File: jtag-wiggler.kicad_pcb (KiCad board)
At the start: 2 copper layers, 152.4 x 101.6 mm, 50 parts, among them J1 DSUB-25_Male_Horizontal_P2.77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, J2 BarrelJack_Horizontal, P1 PinHeader_1x02_P2.54mm_Vertic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, P2 PinHeader_1x03_P2.54mm_Vertic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, P3 PinHeader_1x08_P2.54mm_Vertic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, Q1 TO-92_Wide, SW1 SW_NKK_G1xJP, U1 DIP-20_W7.62mm_Socket_LongPads, U2 TO-220-3_Vertical, U3 TO-220-3_Vertical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

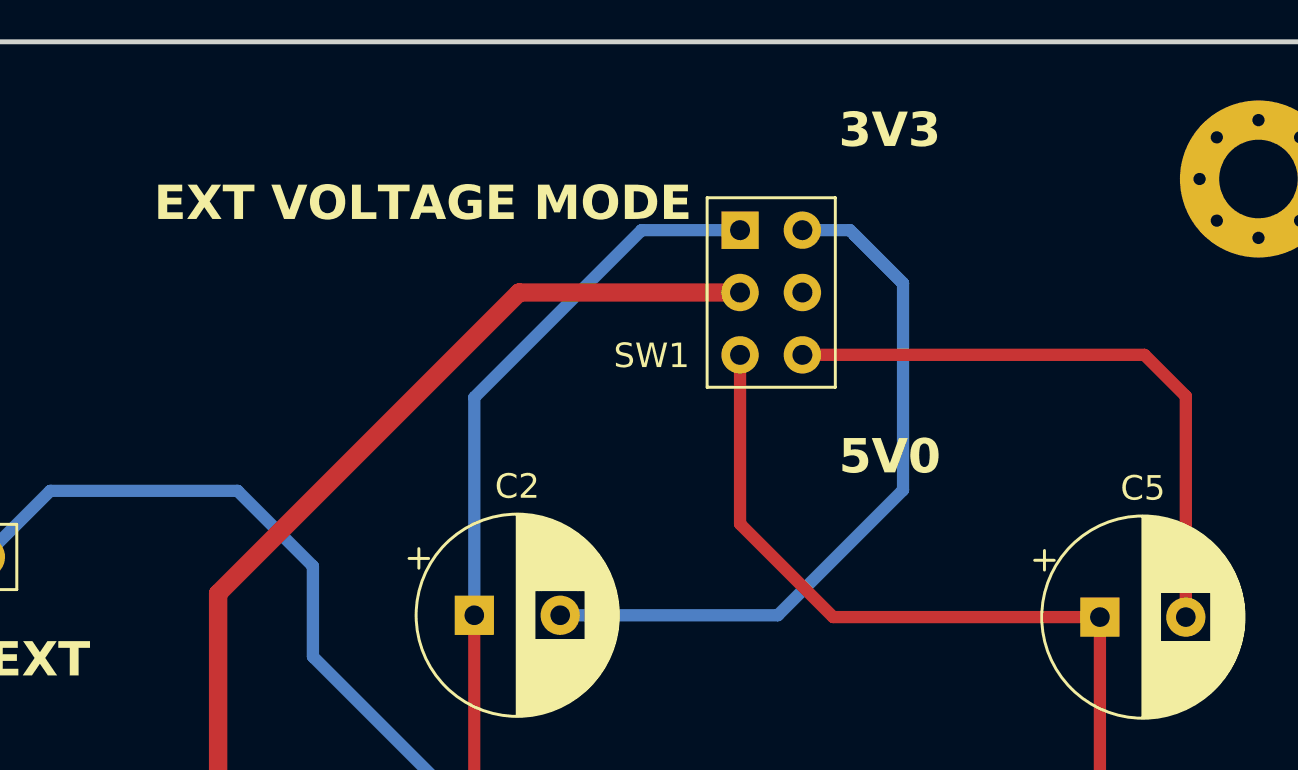
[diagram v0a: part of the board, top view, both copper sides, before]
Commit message: Add custom switch footprint; update PCB layout
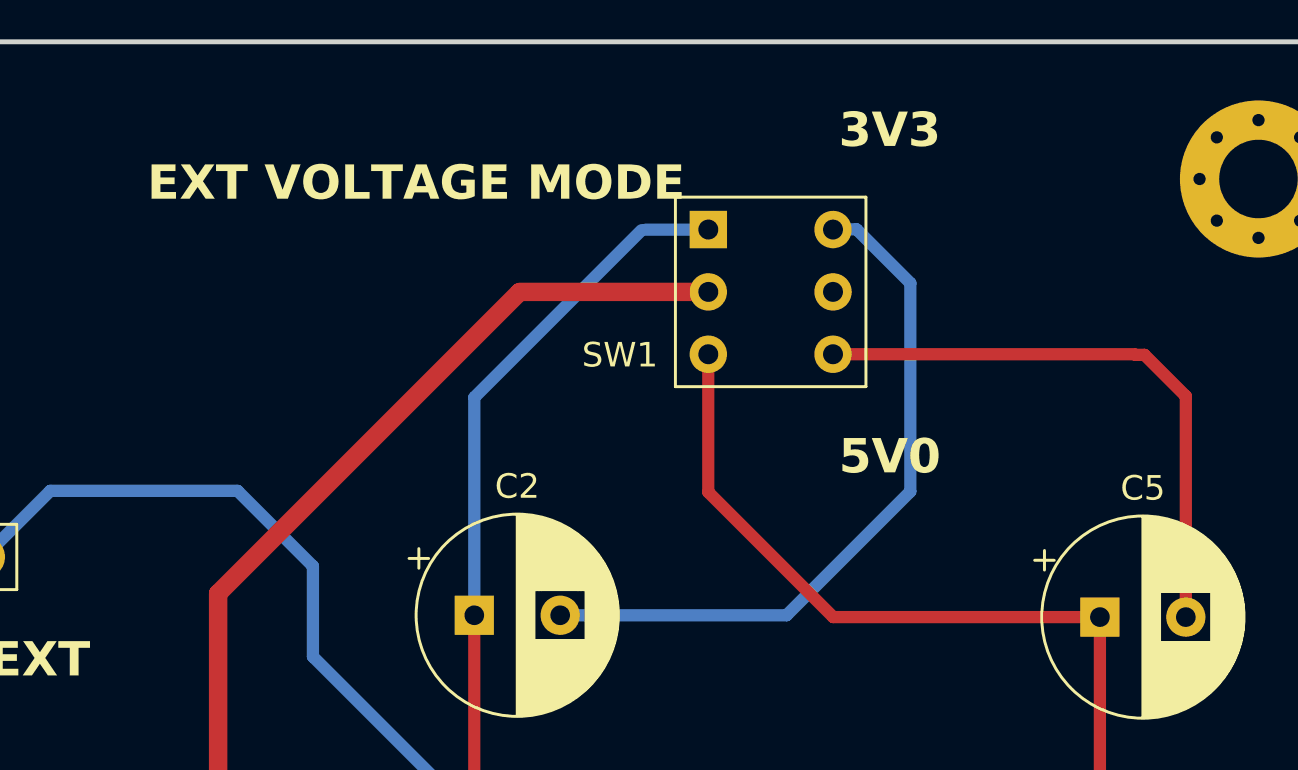
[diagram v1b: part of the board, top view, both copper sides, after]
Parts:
- SW1: value SW_NKK_G1xJP -> SW_Generic; footprint Button_Switch_THT:SW_NKK_G1xJP -> Switches:SW_Generic
- moved SW1 1.29 mm to (198.2, 55.9)
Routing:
- net C2_negative: track 32.3 -> 28.9 mm
- net C2_positive: track 46.7 -> 45.2 mm
- net Protected_VCC: track 74.7 -> 73.5 mm
- net C5_negative: track 25.3 -> 24.1 mm
- net C5_positive: track 34.7 -> 35.3 mm
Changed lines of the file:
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@@
     )
   )
-  (footprint "Button_Switch_THT:SW_NKK_G1xJP" (layer "F.Cu")
-    (at 199.477707 55.935)
-    (descr "Switch NKK G1xJP http://www.nkkswitches.com/pdf/gwillum.pdf")
-    (tags "SWITCH TOGGLE ILLUM SPDT NKK")
+  (footprint "Switches:SW_Generic" (layer "F.Cu")
+    (at 198.185 55.91)
+    (descr "Generic Switch - 2.54mm x 5.08mm spacing")
+    (tags "SWITCH TOGGLE DPDT")
     (attr through_hole)
     (fp_text reference "SW1" (at -3.602707 5.115) (layer "F.SilkS")
         (effects (font (size 1 1) (thickness 0.15)))
     )
-    (fp_text value "SW_NKK_G1xJP" (at 1.27 7.3) (layer "F.Fab")
+    (fp_text value "SW_Generic" (at 2.54 7.3) (layer "F.Fab")
         (effects (font (size 1 1) (thickness 0.15)))
     )
-    (fp_text user "${REFERENCE}" (at 1.27 -2.2) (layer "F.Fab")
+    (fp_text user "${REFERENCE}" (at 2.54 -2.2) (layer "F.Fab")
         (effects (font (size 1 1) (thickness 0.15)))
     )
-    (fp_line (start -1.34112 -1.3208) (end 3.88112 -1.3208)
+    (fp_line (start -1.34112 -1.3208) (end 6.42112 -1.3208)
       (stroke (width 0.12) (type solid)) (layer "F.SilkS"))
     (fp_line (start -1.34112 6.4008) (end -1.34112 -1.3208)
       (stroke (width 0.12) (type solid)) (layer "F.SilkS"))
-    (fp_line (start -1.34112 6.4008) (end 3.88112 6.4008)
+    (fp_line (start -1.34112 6.4008) (end 6.42112 6.4008)
       (stroke (width 0.12) (type solid)) (layer "F.SilkS"))
-    (fp_line (start 3.88112 -1.3208) (end 3.88112 6.4008)
+    (fp_line (start 6.42112 -1.3208) (end 6.42112 6.4008)
       (stroke (width 0.12) (type solid)) (layer "F.SilkS"))
     (fp_line (start -1.48 6.54) (end -1.48 -1.46)
       (stroke (width 0.05) (type solid)) (layer "F.CrtYd"))
-    (fp_line (start -1.48 6.54) (end 4.02 6.54)
+    (fp_line (start -1.48 6.54) (end 6.56 6.54)
       (stroke (width 0.05) (type solid)) (layer "F.CrtYd"))
-    (fp_line (start 4.02 -1.46) (end -1.48 -1.46)
+    (fp_line (start 6.56 -1.46) (end -1.48 -1.46)
       (stroke (width 0.05) (type solid)) (layer "F.CrtYd"))
-    (fp_line (start 4.02 -1.46) (end 4.02 6.54)
+    (fp_line (start 6.56 -1.46) (end 6.56 6.54)
       (stroke (width 0.05) (type solid)) (layer "F.CrtYd"))
-    (fp_line (start -1.23 -1.21) (end 3.77 -1.21)
+    (fp_line (start -1.23 -1.21) (end 6.31 -1.21)
       (stroke (width 0.1) (type solid)) (layer "F.Fab"))
     (fp_line (start -1.23 6.29) (end -1.23 -1.21)
       (stroke (width 0.1) (type solid)) (layer "F.Fab"))
-    (fp_line (start -1.23 6.29) (end 3.77 6.29)
+    (fp_line (start -1.23 6.29) (end 6.31 6.29)
       (stroke (width 0.1) (type solid)) (layer "F.Fab"))
-    (fp_line (start 3.77 6.29) (end 3.77 -1.21)
+    (fp_line (start 6.31 6.29) (end 6.31 -1.21)
       (stroke (width 0.1) (type solid)) (layer "F.Fab"))
     (pad "1" thru_hole rect (at 0 0) (size 1.524 1.524) (drill 0.8128) (layers "*.Cu" "*.Mask")
@@
     (pad "3" thru_hole circle (at 0 5.08) (size 1.524 1.524) (drill 0.8128) (layers "*.Cu" "*.Mask")
       (net 24 "C5_positive"))
-    (pad "4" thru_hole circle (at 2.54 5.08) (size 1.524 1.524) (drill 0.8128) (layers "*.Cu" "*.Mask")
+    (pad "4" thru_hole circle (at 5.08 5.08) (size 1.524 1.524) (drill 0.8128) (layers "*.Cu" "*.Mask")
       (net 26 "C5_negative"))
-    (pad "5" thru_hole circle (at 2.54 2.54) (size 1.524 1.524) (drill 0.8128) (layers "*.Cu" "*.Mask")
+    (pad "5" thru_hole circle (at 5.08 2.54) (size 1.524 1.524) (drill 0.8128) (layers "*.Cu" "*.Mask")
       (net 3 "GND"))
-    (pad "6" thru_hole circle (at 2.54 0) (size 1.524 1.524) (drill 0.8128) (layers "*.Cu" "*.Mask")
+    (pad "6" thru_hole circle (at 5.08 0) (size 1.524 1.524) (drill 0.8128) (layers "*.Cu" "*.Mask")
       (net 25 "C2_negative"))
     (model "${KICAD6_3DMODEL_DIR}/Button_Switch_THT.3dshapes/SW_NKK_G1xJP.wrl"
@@
     (effects (font (size 1.4 1.4) (thickness 0.28) bold) (justify left bottom))
   )
-  (gr_text "EXT VOLTAGE MODE" (at 175.6 55.65) (layer "F.SilkS")
+  (gr_text "EXT VOLTAGE MODE" (at 175.325 54.825) (layer "F.SilkS")
     (effects (font (size 1.4 1.4) (thickness 0.28) bold) (justify left bottom))
   )
@@
   (segment (start 178.2125 70.7375) (end 190.475 58.475) (width 0.75) (layer "F.Cu") (net 1))
   (segment (start 178.2125 114.2875) (end 178.2125 70.7375) (width 0.75) (layer "F.Cu") (net 1))
-  (segment (start 190.475 58.475) (end 199.477707 58.475) (width 0.75) (layer "F.Cu") (net 1))
+  (segment (start 198.185 58.45) (end 190.5 58.45) (width 0.75) (layer "F.Cu") (net 1))
+  (segment (start 190.5 58.45) (end 190.475 58.475) (width 0.25) (layer "F.Cu") (net 1))
   (segment (start 174.8 117.7) (end 178.2125 114.2875) (width 0.75) (layer "F.Cu") (net 1))
   (segment (start 174.85 127.925) (end 174.8 127.875) (width 0.5) (layer "F.Cu") (net 2))
@@
   (segment (start 194.8 93.275) (end 194.8 88.6) (width 0.5) (layer "F.Cu") (net 10))
   (segment (start 188.65 82.45) (end 188.65 71.625) (width 0.5) (layer "F.Cu") (net 10))
+  (segment (start 198.185 55.91) (end 195.65 55.91) (width 0.5) (layer "B.Cu") (net 10))
   (segment (start 188.65 62.75) (end 188.65 71.625) (width 0.5) (layer "B.Cu") (net 10))
   (segment (start 195.465 55.935) (end 188.65 62.75) (width 0.5) (layer "B.Cu") (net 10))
-  (segment (start 199.477707 55.935) (end 195.465 55.935) (width 0.5) (layer "B.Cu") (net 10))
   (segment (start 159.775 98.875) (end 159.795 98.895) (width 0.5) (layer "F.Cu") (net 11))
   (segment (start 132.55 71.65) (end 132.55 62.05) (width 0.5) (layer "F.Cu") (net 11))
@@
   (segment (start 87.475 91.55) (end 86.425 90.5) (width 0.5) (layer "B.Cu") (net 23))
   (segment (start 86.425 90.5) (end 84.44 90.5) (width 0.5) (layer "B.Cu") (net 23))
-  (segment (start 199.477707 61.015) (end 199.477707 67.902707) (width 0.5) (layer "F.Cu") (net 24))
+  (segment (start 198.185 60.99) (end 198.185 66.61) (width 0.5) (layer "F.Cu") (net 24))
+  (segment (start 203.275 71.7) (end 214.140056 71.7) (width 0.5) (layer "F.Cu") (net 24))
   (segment (start 214.140056 83.044944) (end 214.065 83.12) (width 0.5) (layer "F.Cu") (net 24))
   (segment (start 214.140056 83.075) (end 214.040056 83.175) (width 0.5) (layer "F.Cu") (net 24))
   (segment (start 214.140056 71.7) (end 214.140056 83.044944) (width 0.5) (layer "F.Cu") (net 24))
-  (segment (start 199.477707 67.902707) (end 203.275 71.7) (width 0.5) (layer "F.Cu") (net 24))
-  (segment (start 203.275 71.7) (end 214.140056 71.7) (width 0.5) (layer "F.Cu") (net 24))
-  (segment (start 206.117707 66.524999) (end 206.117707 58.100001) (width 0.5) (layer "B.Cu") (net 25))
-  (segment (start 204.133853 56.116147) (end 203.952707 55.935) (width 0.5) (layer "B.Cu") (net 25))
-  (segment (start 201.017706 71.625) (end 206.117707 66.524999) (width 0.5) (layer "B.Cu") (net 25))
-  (segment (start 203.952707 55.935) (end 202.017707 55.935) (width 0.5) (layer "B.Cu") (net 25))
-  (segment (start 201.017706 71.625) (end 192.15 71.625) (width 0.5) (layer "B.Cu") (net 25))
-  (segment (start 206.117707 58.1) (end 204.133853 56.116147) (width 0.5) (layer "B.Cu") (net 25))
-  (segment (start 206.117707 58.100001) (end 204.133853 56.116147) (width 0.5) (layer "B.Cu") (net 25))
+  (segment (start 198.185 66.61) (end 203.275 71.7) (width 0.5) (layer "F.Cu") (net 24))
+  (segment (start 201.374999 71.625) (end 192.15 71.625) (width 0.5) (layer "B.Cu") (net 25))
+  (segment (start 203.265 55.91) (end 203.273853 55.901147) (width 0.5) (layer "B.Cu") (net 25))
+  (segment (start 203.273853 55.901147) (end 204.226146 55.901147) (width 0.5) (layer "B.Cu") (net 25))
+  (segment (start 206.416147 58.091148) (end 206.416147 66.583852) (width 0.5) (layer "B.Cu") (net 25))
+  (segment (start 204.226146 55.901147) (end 206.416147 58.091148) (width 0.5) (layer "B.Cu") (net 25))
+  (segment (start 206.416147 66.583852) (end 201.374999 71.625) (width 0.5) (layer "B.Cu") (net 25))
+  (segment (start 215.575 61.015) (end 215.955 61.015) (width 0.5) (layer "F.Cu") (net 26))
+  (segment (start 215.55 60.99) (end 215.575 61.015) (width 0.25) (layer "F.Cu") (net 26))
+  (segment (start 203.265 60.99) (end 215.55 60.99) (width 0.5) (layer "F.Cu") (net 26))
   (segment (start 215.955 61.015) (end 217.640056 62.700056) (width 0.5) (layer "F.Cu") (net 26))
-  (segment (start 202.017707 61.015) (end 215.955 61.015) (width 0.5) (layer "F.Cu") (net 26))
   (segment (start 217.640056 62.700056) (end 217.640056 71.7) (width 0.5) (layer "F.Cu") (net 26))
   (segment (start 140.225 89.375) (end 140.17 89.32) (width 0.5) (layer "F.Cu") (net 29))
